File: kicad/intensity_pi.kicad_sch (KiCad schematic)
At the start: 68 parts, among them J1 Input A, J2 Input B / Setpoint, J3 Monitor, J4 Output, J7 select 1, SW1 SW_SPDT, SW2 SW_SPDT, SW3 SW_SPDT, SW5 SW_DP3T, U1 LM4040DBZ-5, U10 OPA189, U11 PC817, U12 OPA189, U13 BUF634A, U14 TMUX6123, U17 TMUX6123, U18 OPA189, U2 LM4040DBZ-5, U20 OPA189, U3 INA849, U4 INA849, U5 OPA189, U7 OPA189, U8 BUF634A

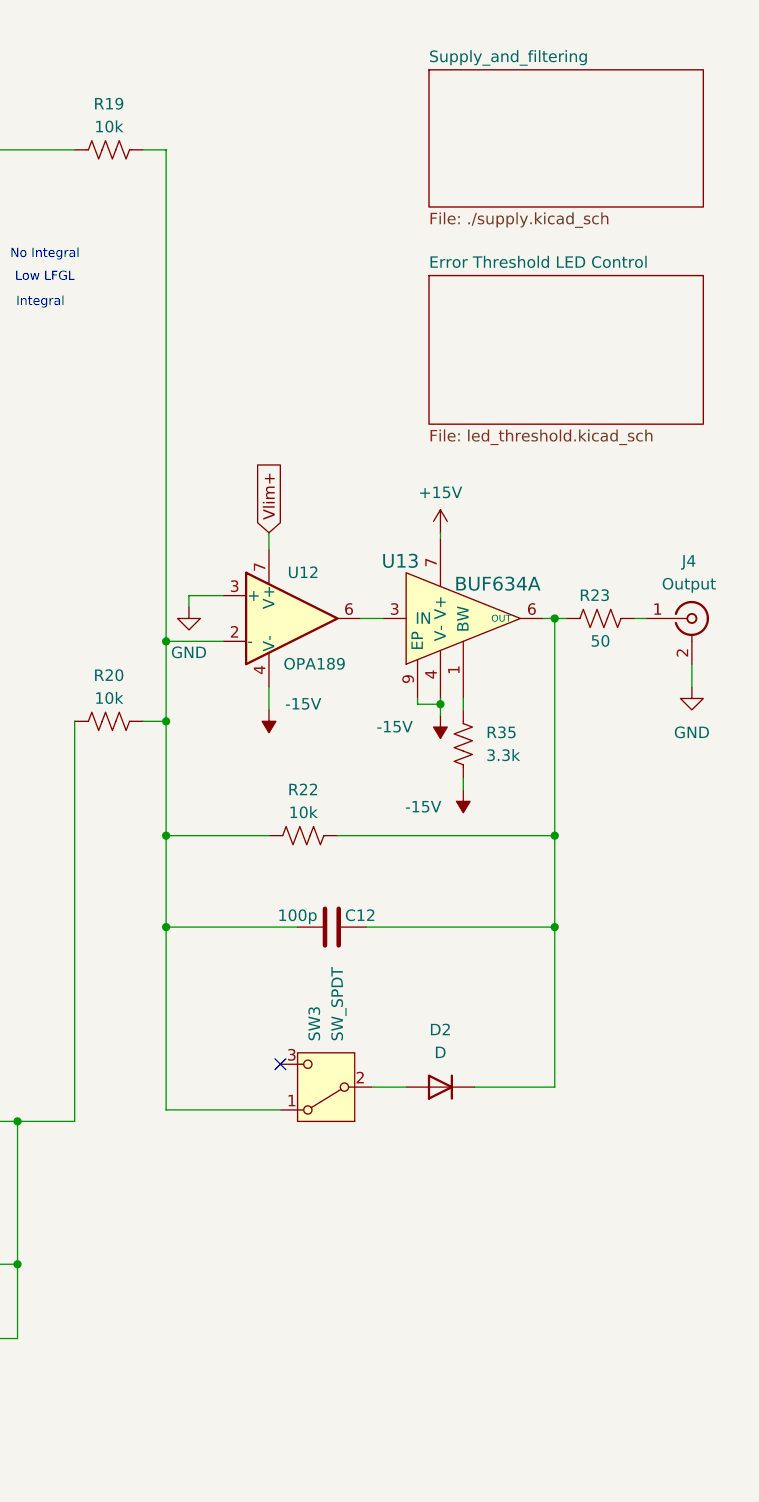
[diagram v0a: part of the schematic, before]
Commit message: First pass at schematic for updated bidirectional clamping and output offset when the lock is turned off, no layout changes yet
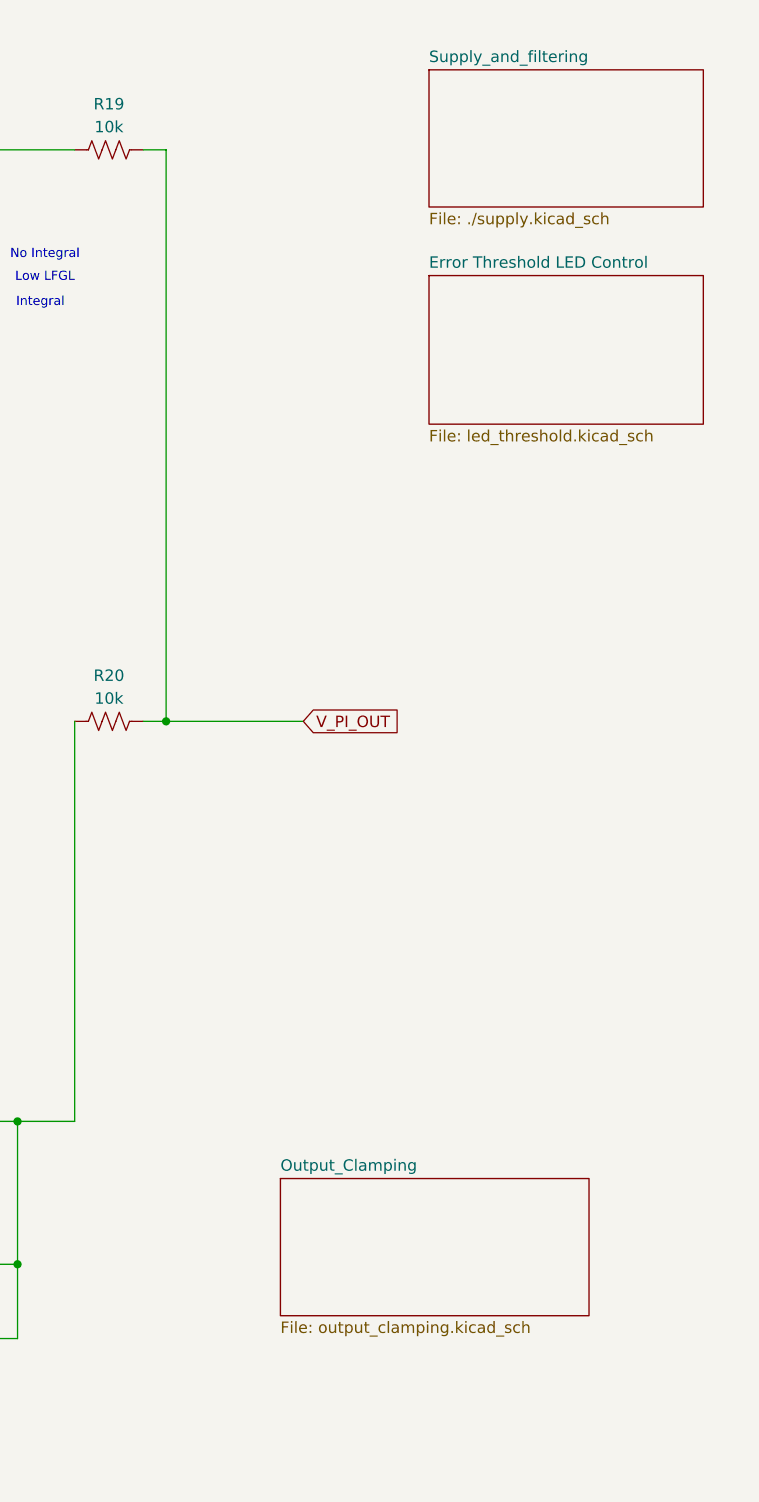
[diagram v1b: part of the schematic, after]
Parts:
- removed C12: 100p, Capacitor_SMD:C_0805_2012Metric, symbol Device:C
- removed D2: D, Package_TO_SOT_SMD:TSOT-23, symbol Device:D
- removed J4: Output, Connector_Coaxial:BNC_Amphenol_B6252HB-NPP3G-50_Horizontal, symbol Connector:Conn_Coaxial
- removed R22: 10k, Resistor_SMD:R_0805_2012Metric, symbol Device:R_US
- removed R23: 50, Resistor_SMD:R_0805_2012Metric, symbol Device:R_US
- removed R35: 3.3k, Resistor_SMD:R_0805_2012Metric, symbol Device:R_US
- removed SW3: SW_SPDT, Custom_Footprints:TDD DIP Switch, symbol Switch:SW_SPDT
- removed U12: OPA189, Package_SO:SOIC-8_3.9x4.9mm_P1.27mm, symbol Amplifier_Operational:OPA330xxD
- removed U13: BUF634A, lib:TI_SO-PowerPAD-8_ThermalVias, symbol local_lib:BUF634A
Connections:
- net V_PI_OUT: now reaches R19.2, R20.2
- no-connect marks 4 -> 3
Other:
- added sheet Output_Clamping (output_clamping.kicad_sch)

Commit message: Updated schematic and design
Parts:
- added J5: Sweep IN, Connector_Coaxial:BNC_Amphenol_B6252HB-NPP3G-50_Horizontal, symbol Connector:Conn_Coaxial
- added R18, R25, R54, R56, R57: 10k, Resistor_SMD:R_0805_2012Metric, symbol Device:R_US
- added R52: 1k, Resistor_SMD:R_0805_2012Metric, symbol Device:R_US
- added R53: DNP, Resistor_SMD:R_0805_2012Metric, symbol Device:R_US
- added R55: 5k, Resistor_SMD:R_0805_2012Metric, symbol Device:R_US
- added RV2: 100k, Custom_Footprints:Bourns Circular Pots, symbol Device:R_Potentiometer_US
- added U33: INA849, Package_SO:SOIC-8_3.9x4.9mm_P1.27mm, symbol Amplifier_Instrumentation:AD8236
- added U6: OPA189, Package_SO:SOIC-8_3.9x4.9mm_P1.27mm, symbol Amplifier_Operational:OPA330xxD
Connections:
- net +15V: now also U33.8 (Vs+), U6.7 (V+)
- net -15V: now also U33.5 (Vs-), U6.4 (V-)
- net GND: now also R52.1, R57.1, U33.6 (Ref)
- net V_PI_OUT: now also R25.2, U6.6; no longer R19.2, R20.2
- new net: R55.1, R57.2, RV2.3
- new net: R19.2, R20.2, R54.2, R55.2, U6.3 (+)
- new net: J5.2 (Ext), R18.1, R52.2, U33.1 (-)
- new net: R53.2, U33.2 (Rg)
- new net: R53.1, U33.3 (Rg)
- new net: J5.1 (In), R18.2, U33.4 (+)
- new net: R25.1, U6.2 (-)
- new net: R56.2, RV2.1, RV2.2
- new net OUTPUT_OFFSET: R54.1
- new net Sweep_IN: R56.1, U33.7
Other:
- moved on the sheet: R13, R16, RV3, U10, U17B

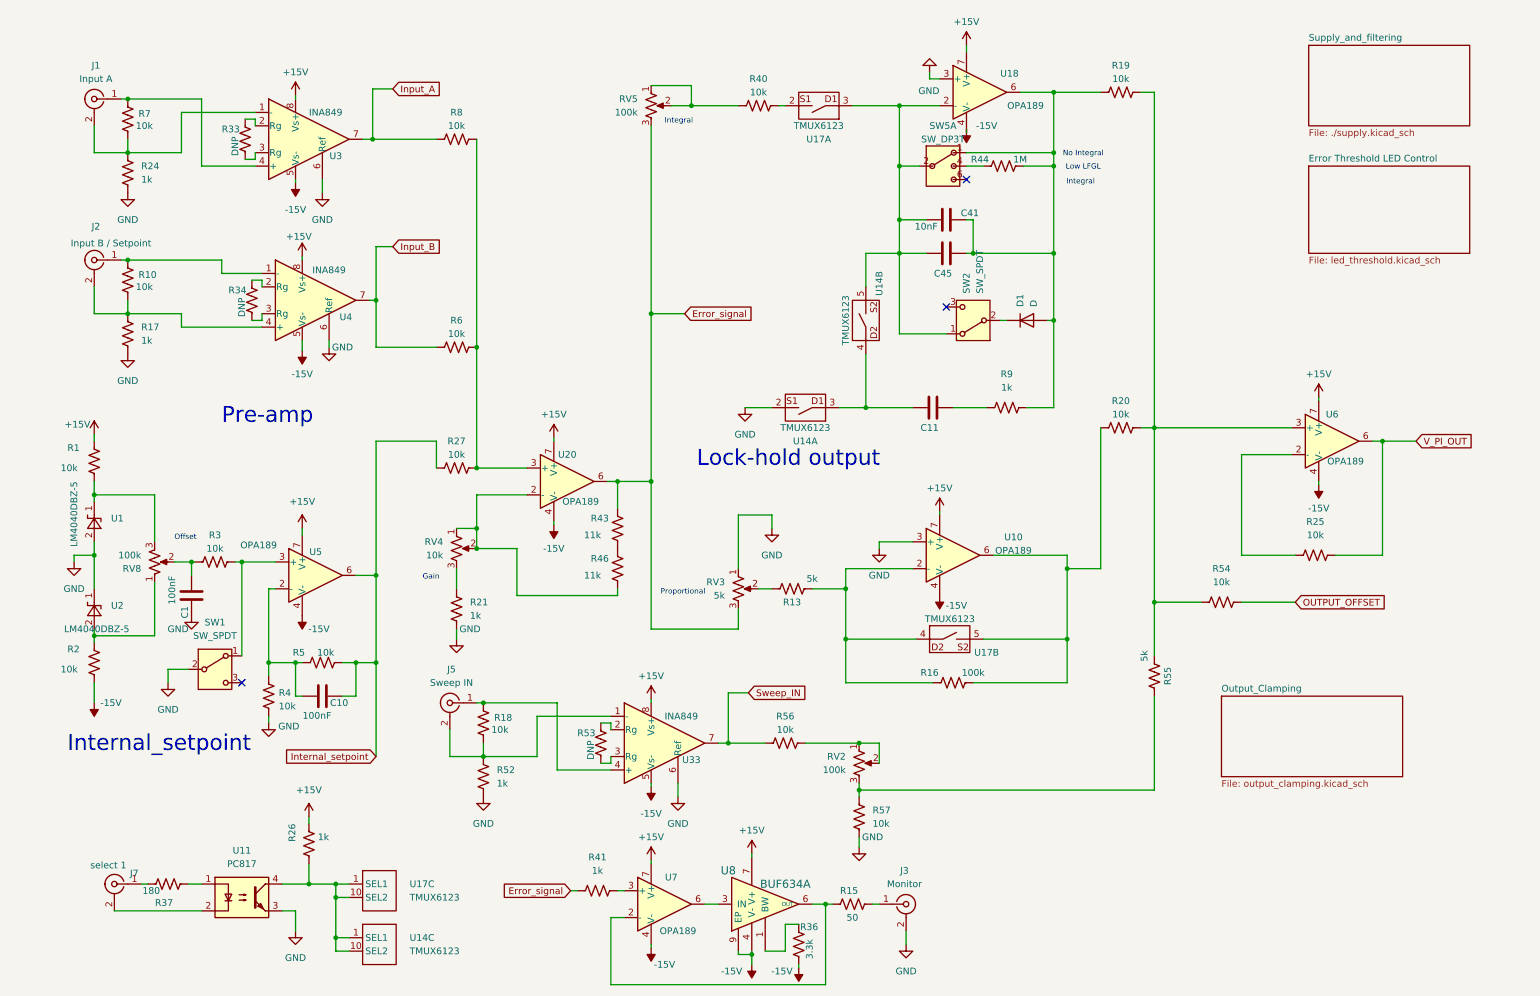
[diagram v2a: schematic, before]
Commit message: First pass at updated schematic and loose PCB grouping, TODO: Fix PI Gain values
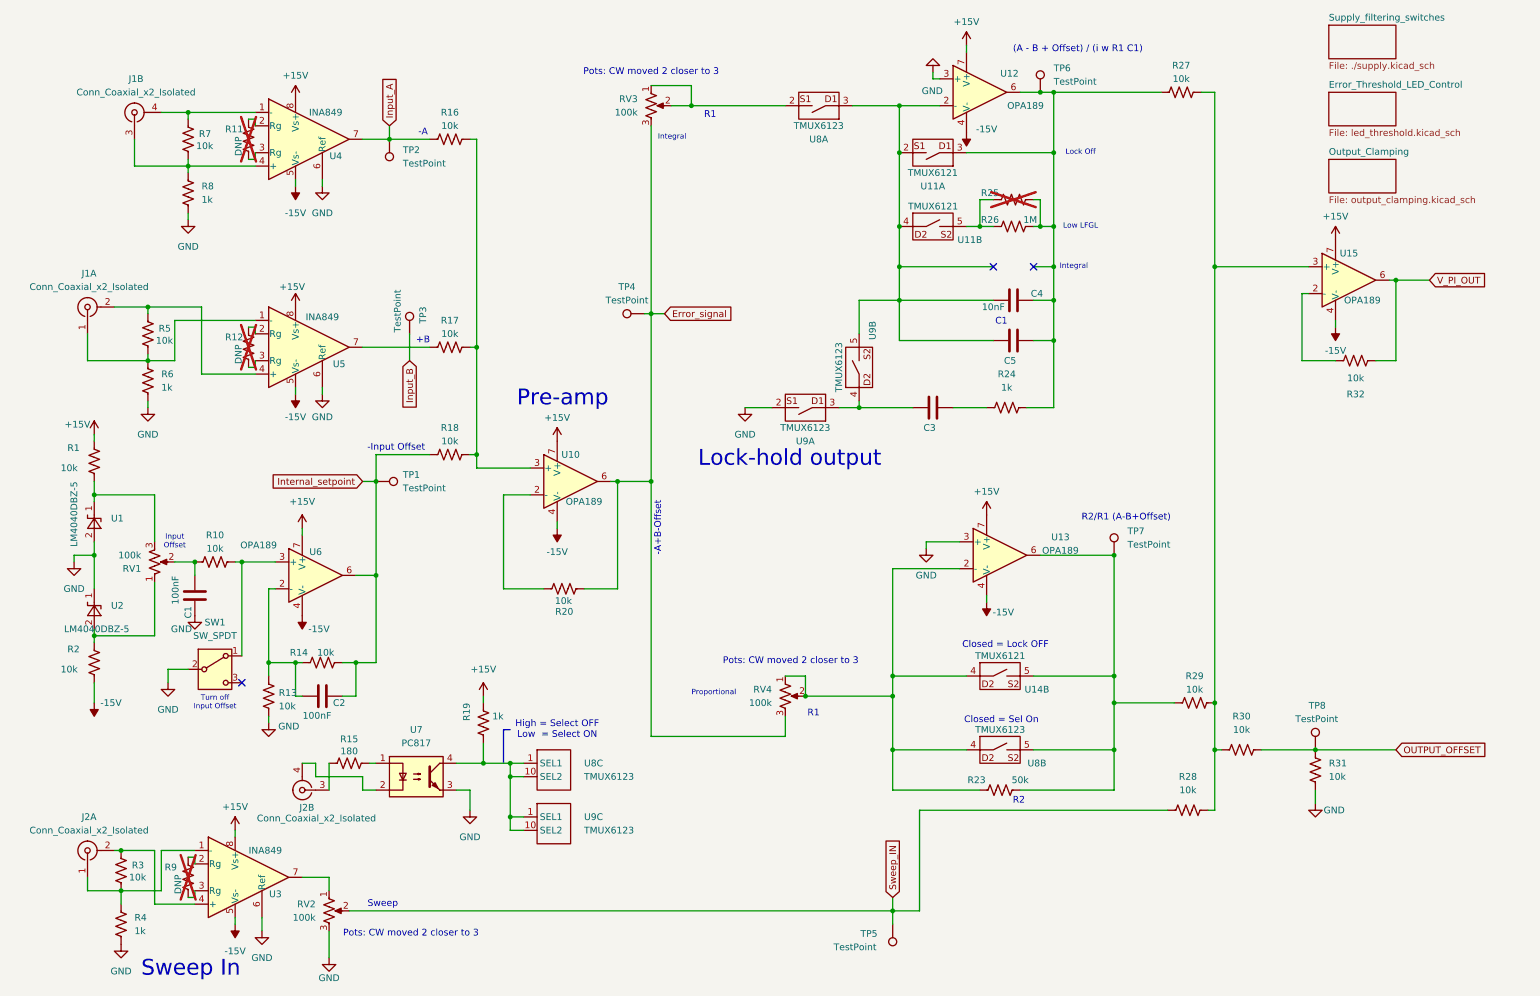
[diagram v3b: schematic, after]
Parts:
- removed D1: D, Package_TO_SOT_SMD:TSOT-23, symbol Device:D
- removed J1: Input A, Connector_Coaxial:BNC_Amphenol_B6252HB-NPP3G-50_Horizontal, symbol Connector:Conn_Coaxial
- removed J2: Input B / Setpoint, Connector_Coaxial:BNC_Amphenol_B6252HB-NPP3G-50_Horizontal, symbol Connector:Conn_Coaxial
- removed J3: Monitor, Connector_Coaxial:BNC_Amphenol_B6252HB-NPP3G-50_Horizontal, symbol Connector:Conn_Coaxial
- removed J5: Sweep IN, Connector_Coaxial:BNC_Amphenol_B6252HB-NPP3G-50_Horizontal, symbol Connector:Conn_Coaxial
- removed J7: select 1, Connector_Coaxial:BNC_Amphenol_B6252HB-NPP3G-50_Horizontal, symbol Connector:Conn_Coaxial
- removed R13, R55: 5k, Resistor_SMD:R_0805_2012Metric, symbol Device:R_US
- removed R21, R26, R41: 1k, Resistor_SMD:R_0805_2012Metric, symbol Device:R_US
- removed R36: 3.3k, Resistor_SMD:R_0805_2012Metric, symbol Device:R_US
- removed R37: 180, Resistor_SMD:R_0805_2012Metric, symbol Device:R_US
- removed R40, R56, R57: 10k, Resistor_SMD:R_0805_2012Metric, symbol Device:R_US
- removed R46: 11k, Resistor_SMD:R_0805_2012Metric, symbol Device:R_US
- removed RV3: 5k, Custom_Footprints:Bourns Circular Pots, symbol Device:R_Potentiometer_US
- removed SW2: SW_SPDT, Custom_Footprints:TDD DIP Switch, symbol Switch:SW_SPDT
- removed SW5: SW_DP3T, Custom_Footprints:Right Angle 3PDT Switch, symbol Custom_Symbols:DP3T_1
- removed U11: PC817, Package_DIP:DIP-4_W7.62mm, symbol Isolator:PC817
- removed unit 3 of U14
- removed unit 3 of U17
- removed U7: OPA189, Package_SO:SOIC-8_3.9x4.9mm_P1.27mm, symbol Amplifier_Operational:OPA330xxD
- removed U8: BUF634A, lib:TI_SO-PowerPAD-8_ThermalVias, symbol local_lib:BUF634A
- added J1, J2: Conn_Coaxial_x2_Isolated, Connector_Coaxial:BNC_Amphenol_031-6575_Horizontal, symbol Connector:Conn_Coaxial_x2_Isolated
- added R19: 1k, Resistor_SMD:R_0805_2012Metric, symbol Device:R_US
- added R25: (no value), Resistor_THT:R_Axial_DIN0204_L3.6mm_D1.6mm_P7.62mm_Horizontal, symbol Device:R_US
- added R28, R31: 10k, Resistor_SMD:R_0805_2012Metric, symbol Device:R_US
- added TP1, TP2, TP3, TP4, TP5, TP6, TP7, TP8: TestPoint, TestPoint:TestPoint_Loop_D2.60mm_Drill1.6mm_Beaded, symbol Connector:TestPoint
- added U11, U14: TMUX6121, Custom_Footprints:TMUX6121, symbol library_intensity_pi:TMUX6123_split
- added U7: PC817, Package_DIP:DIP-4_W7.62mm, symbol Isolator:PC817
- added unit 3 of U8
- added unit 3 of U9
- R11: renamed from R33; now not fitted
- R12: renamed from R34; now not fitted
- R15: value 50 -> 180; DIGIKEY 541-CRCW080550R0FKTACT-ND -> CR0805-FX-1800ELFCT-ND; PARTNO CRCW080550R0FKTA -> CR0805-FX-1800ELF
- R20: renamed from R43; value 11k -> 10k
- R23: renamed from R16; value 100k -> 50k; DIGIKEY P100KDACT-ND -> (none); PARTNO ERA-6AEB104V -> (none)
- R9: renamed from R53; now not fitted
- RV1: renamed from RV8; Tag (none) -> Input Offset
- RV2: Tag (none) -> Sweep Amp
- RV3: renamed from RV5; Tag (none) -> Integral Gain
- RV4: value 10k -> 100k; DIGIKEY 3590S-2-103L-ND -> 3590P-2-104L-ND; PARTNO 3590S-2-103L -> 3590P-2-104L; Tag (none) -> Proportional Gain
- SW1: footprint Custom_Footprints:Right Angle SPDT Switch -> Custom_Footprints:Right Angle SPDT Vertical; DIGIKEY EG2362-ND -> 100SP1T1B1M7QEH-ND; PARTNO 100SP1T2B4M6QE -> 100SP1T1B1M7QEH; Tag (none) -> Input Offset Toggle
- U8: renamed from U17; footprint Package_SO:VSSOP-10_3x3mm_P0.5mm -> Custom_Footprints:TMUX6123
- U9: renamed from U14; footprint Package_SO:VSSOP-10_3x3mm_P0.5mm -> Custom_Footprints:TMUX6123
- renumbered C10 to C2, C11 to C3, C41 to C4, C45 to C5, R3 to R10, R4 to R13, R5 to R14, R8 to R16, R6 to R17, R27 to R18, R9 to R24, R44 to R26, R19 to R27, R20 to R29, R18 to R3, R54 to R30, R25 to R32, R52 to R4, R10 to R5, R17 to R6, R24 to R8, U20 to U10, U18 to U12, U10 to U13, U6 to U15, U33 to U3, U3 to U4, U4 to U5, U5 to U6
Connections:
- net +15V: now also R19.1
- net Error_signal: now also R20.1, RV4.3, TP4.1; no longer R20.2
- net GND: now also RV2.3, R31.2, U7.3
- net Input_A: now also TP2.1
- net Input_B: now also TP3.1; no longer R17.1, U5.7
- net Internal_setpoint: now also TP1.1
- net OUTPUT_OFFSET: now also R31.1, TP8.1
- net Sweep_IN: now also RV2.2, R28.1, TP5.1; no longer U3.7
- net V_PI_OUT: now also R32.1; no longer R32.2
- net at R27.2, R29.2, R30.2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: now also R28.2
- net at R7.1, R8.2: now also U4.4 (+), J1.3 (In2); no longer U4.1 (-)
- net at R7.2: now also U4.1 (-), J1.4 (Ext2); no longer U4.4 (+)
- net at R3.1, R4.2, U3.1 (-): now also J2.1 (In1)
- net at R3.2, U3.4 (+): now also J2.2 (Ext1)
- net at C4.1, C5.2, R24.1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: now also R25.2, TP6.1, U11.3
- net at R23.1, U13.2 (-), U8.4: now also RV4.1, RV4.2, U14.4
- net at R23.2, R29.1, U13.6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: now also TP7.1, U14.5
- net at C4.2, C5.1, U12.2 (-)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: now also U11.2, U11.4
- net at R26.1: now also R25.1, U11.5
- net at R5.1, R6.2: now also U5.1 (-), J1.1 (In1); no longer U5.4 (+)
- net at R5.2: now also U5.4 (+), J1.2 (Ext1); no longer U5.1 (-)
- net at RV3.1, RV3.2: now also U8.2
- net at R15.1: now also U7.1
- net at R15.2: now also J2.3 (In2)
- net at U15.2 (-): now also R32.2; no longer R32.1
- net at RV2.1: now also U3.7; no longer RV2.2
- new net: R19.2, U7.4, U8.1 (SEL1), U8.10 (SEL2), U9.1 (SEL1), U9.10 (SEL2)
- new net: R20.2, U10.2 (-)
- new net: R17.1, U5.7
- new net: J2.4 (Ext2), U7.2
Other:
- sheet Error Threshold LED Control renamed Error_Threshold_LED_Control
- sheet Supply_and_filtering renamed Supply_filtering_switches
- note added: "(A - B + Offset) / (i w R1 C1)"
- note added: "+B"
- note added: "-A"
- note added: "-A+B-Offset"
- note added: "-Input Offset"
- note added: "C1"
- note added: "Closed = Lock OFF"
- note added: "Closed = Sel On"
- note added: "High = Select OFF Low = Select ON"
- note added: "Input Offset"
- note added: "Lock Off"
- note added: "Pots: CW moved 2 closer to 3"
- note added: "R1"
- note added: "R2"
- note added: "R2/R1 (A-B+Offset)"
- note added: "Sweep"
- note added: "Sweep In"
- note added: "Turn off Input Offset"
- note removed: "Gain"
- note removed: "Internal_setpoint"
- note removed: "No Integral"
- note removed: "Offset"
- moved on the sheet: C1, C4, C5, R16, R17, R18, R20, R23, R26, R27, R29, R3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

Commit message: Added Test Board to test various gain control as well as clamping mechanism
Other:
- added sheet Test_Board (test_board.kicad_sch)
- note added: "(A - B + Offset) / (i w RV3 C1)"
- note added: "R23/RV4 (A-B+Offset)"
- note removed: "(A - B + Offset) / (i w R1 C1)"
- note removed: "R1"
- note removed: "R2"
- note removed: "R2/R1 (A-B+Offset)"
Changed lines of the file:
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@@
 		)
 	)
-	(text "R1\n"
-		(exclude_from_sim no)
-		(at 135.636 32.258 0)
-		(effects
-			(font
-				(size 1.27 1.27)
-			)
-		)
-	)
 	(text "Pots: CW moved 2 closer to 3"
 		(exclude_from_sim no)
@@
 		)
 	)
-	(text "(A - B + Offset) / (i w R1 C1)"
+	(text "(A - B + Offset) / (i w RV3 C1)"
 		(exclude_from_sim no)
 		(at 205.232 19.812 0)
@@
 		)
 	)
-	(text "R1"
-		(exclude_from_sim no)
-		(at 155.194 145.542 0)
-		(effects
-			(font
-				(size 1.27 1.27)
-			)
-		)
-	)
 	(text "Closed = Sel On"
 		(exclude_from_sim no)
@@
 		)
 	)
-	(text "R2/R1 (A-B+Offset)"
+	(text "R23/RV4 (A-B+Offset)"
 		(exclude_from_sim no)
 		(at 214.376 108.458 0)
@@
 		)
 	)
-	(text "R2"
-		(exclude_from_sim no)
-		(at 194.056 162.052 0)
-		(effects
-			(font
-				(size 1.27 1.27)
-			)
-		)
-	)
 	(junction
 		(at 74.93 36.83)
@@
 				)
 			)
+		)
+	)
+	(sheet
+		(at 234.315 16.51)
+		(size 12.7 6.35)
+		(exclude_from_sim no)
+		(in_bom yes)
+		(on_board yes)
+		(dnp no)
+		(fields_autoplaced yes)
+		(stroke
+			(width 0.1524)
+			(type solid)
+		)
+		(fill
+			(color 0 0 0 0)
+		)
+		(property "Sheetname" "Test_Board"
+			(at 234.315 15.7984 0)
+			(show_name no)
+			(do_not_autoplace no)
+			(effects
+				(font
+					(size 1.27 1.27)
+				)
+				(justify left bottom)
+			)
+		)
+		(property "Sheetfile" "test_board.kicad_sch"
+			(at 234.315 23.4446 0)
+			(show_name no)
+			(do_not_autoplace no)
+			(effects
+				(font
+					(size 1.27 1.27)
+				)
+				(justify left top)
+			)
+		)
+		(instances
+			(project "intensity_pi"
+				(path "/3a3d7bcb-6fa5-41ef-9ea1-6d4ab7c492fd"
+					(page "5")
+				)
+			)
